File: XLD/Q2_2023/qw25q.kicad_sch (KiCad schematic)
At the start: 521 parts

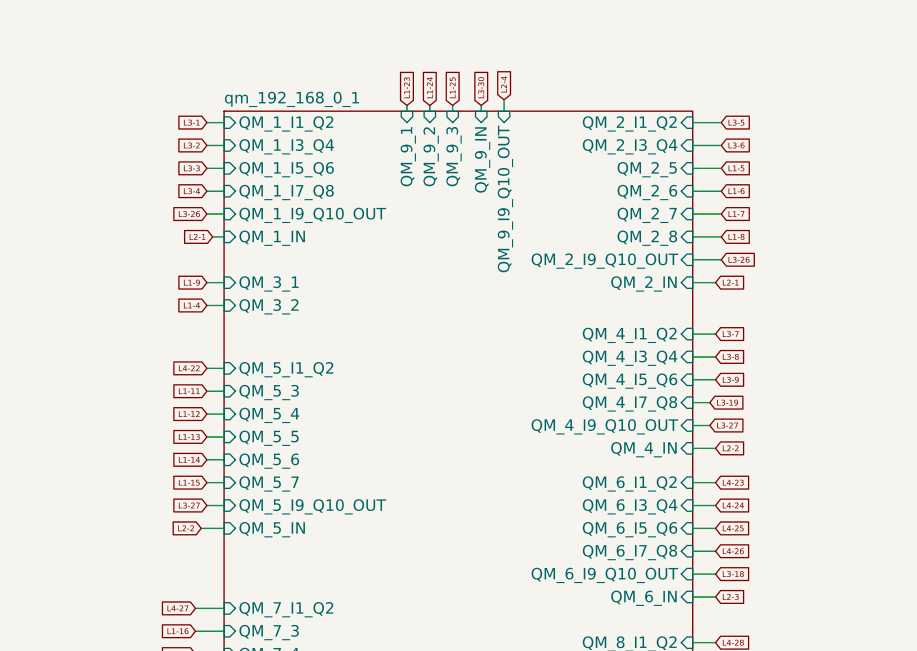
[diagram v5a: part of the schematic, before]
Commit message: connections for qw25q 2 qubit characterization
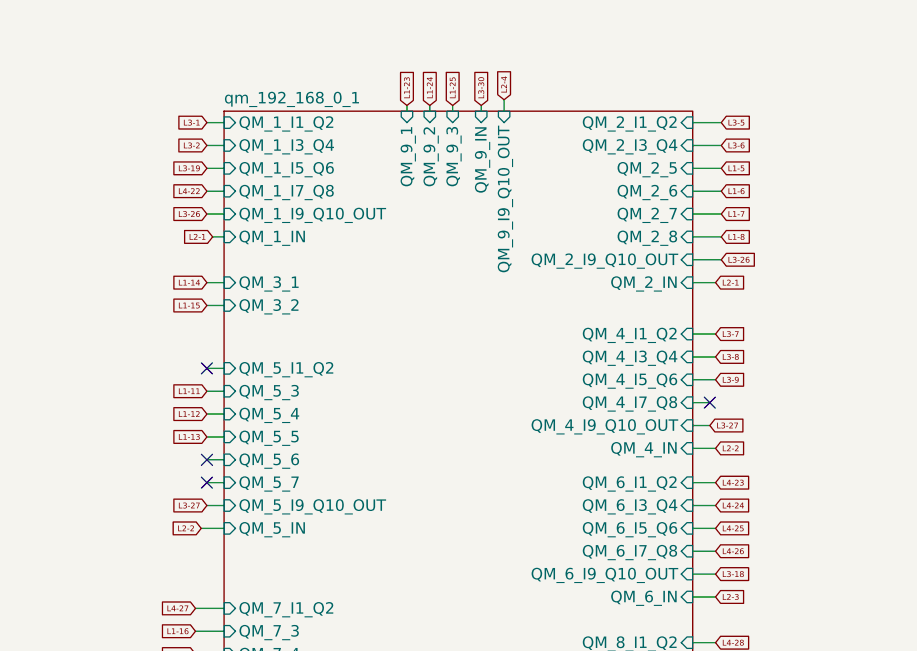
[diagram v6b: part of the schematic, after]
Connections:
- net at EF43.: now also LPF34.; no longer L:96.
- net at EF52.: now also LPF43.; no longer L:104.
- net at EF29.: now also L:5.; no longer LPF20.
- net at EF69.: now also L:153.; no longer LPF60.
- net at Coupler1.: now also L:3.; no longer L:4. (x2)
- net at L:3.: now also TWPA1.; no longer Coupler1.
- net at EF39.: now also LPF30.; no longer L:92.
- net at L:4.: now also Coupler1.; no longer TJI2. (x2)
- net at EF71.: now also LPF62.; no longer L:170.
- net at EF50.: now also L:102.; no longer LPF41.
- net at EF46.: now also L:98.; no longer LPF37.
- net at EF54.: now also L:106.; no longer LPF45.
- net at TJI2.: now also L:4.; no longer L:5.
- net at TWPA1.: now also L:3.; no longer L:2. (x2)
- net at L:3.: now also Coupler1.; no longer TWPA1. (x2)
- net at EF37.: now also L:27.; no longer LPF28.
- net at L:1.: now also TJI1.
- net at TJI1.: now also L:2.; no longer L:1.
- net at L:2.: now also TJI1.; no longer TWPA1. (x2)
- net at TJI1.: now also L:1.; no longer L:2. (x2)
- net at EF70.: now also L:168.; no longer LPF61.
- net at EF33.: now also LPF24.; no longer L:9.
- net at EF31.: now also LPF22.; no longer L:7.
- net at EF64.: now also LPF55.; no longer L:116.
- net at EF27.: now also L:3.; no longer LPF18.
- net at EF62.: now also L:114.; no longer LPF53.
- net at EF68.: now also L:120.; no longer LPF59.
- net at EF66.: now also LPF57.; no longer L:118.
- net at EF41.: now also LPF32.; no longer L:94.
- net at L:4.: now also TJI2.; no longer Coupler1.
- net at EF72.: now also L:174.; no longer LPF63.
- net at L:2.: now also TWPA1.; no longer TJI1.
- net at EF56.: now also L:108.; no longer LPF47.
- net at TJI2.: now also L:5.; no longer L:4.
- net at EF35.: now also L:25.; no longer LPF26.
- net at EF48.: now also L:100.; no longer LPF39.
- net at EF60.: now also LPF51.; no longer L:112.
- net at EF58.: now also LPF49.; no longer L:110.
- new net: EF43., L:96.
- new net: EF52., L:104.
- new net: EF29., LPF20.
- new net: ATT347., ATT348.
- new net: EF69., LPF60.
- new net: Coupler1., L:4. (x2)
- new net: EF39., L:92.
- new net: EF44., LPF35.
- new net: L:4., TJI2.
- new net: EF55., LPF46.
- new net: EF71., L:170.
- new net: EF38., LPF29.
- new net: EF50., LPF41.
- new net: EF46., LPF37.
- new net: EF47., LPF38.
- new net: ATT351., ATT352.
- new net: EF54., LPF45.
- new net: L:5., TJI2.
- new net: L:2., TWPA1. (x3)
- new net: EF37., LPF28.
- new net: EF51., LPF42.
- new net: EF70., LPF61.
- new net: ATT349., ATT350.
- new net: ATT345., ATT346.
- new net: EF65., LPF56.
- new net: EF33., L:9.
- new net: L:6., LX-X2. (x3)
- new net: EF31., L:7.
- new net: EF30., LPF21.
- new net: EF64., L:116.
- new net: EF57., LPF48.
- new net: EF27., LPF18.
- new net: EF49., LPF40.
- new net: EF61., LPF52.
- new net: EF62., LPF53.
- new net: EF68., LPF59.
- new net: EF66., L:118.
- new net: EF41., L:94.
- new net: EF72., LPF63.
- new net: L:2., TJI1.
- new net: EF40., LPF31.
- new net: EF28., LPF19.
- new net: EF56., LPF47.
- new net: EF67., LPF58.
- new net: EF35., LPF26.
- new net: EF63., LPF54.
- new net: EF36., LPF27.
- new net: EF45., LPF36.
- new net: EF53., LPF44.
- new net: EF48., LPF39.
- new net: EF60., L:112.
- new net: EF32., LPF23.
- new net: EF58., L:110.
- new net: EF42., LPF33.
- new net: EF34., LPF25.
- new net: EF59., LPF50.
- no-connect marks 0 -> 4
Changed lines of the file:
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@@
   (junction (at 401.955 142.875) (diameter 0) (color 0 0 0 0)
   )
+  (no_connect (at 730.885 431.8))
+  (no_connect (at 730.885 444.5))
+  (no_connect (at 730.885 441.96))
+  (no_connect (at 786.765 435.61))
   (bus_entry (at 666.75 440.055) (size 2.54 2.54)
     (stroke (width 0) (type default))
@@
     )
   )
-  (global_label "L3-3" (shape input) (at 730.885 409.575 180) (fields_autoplaced)
-    (effects (font (size 0.64 0.64)) (justify right))
-    (property "Intersheetrefs" "${INTERSHEET_REFS}" (at 726.8912 409.575 0)
-      (effects (font (size 1.27 1.27)) (justify right) hide)
-    )
-  )
   (global_label "L2-4" (shape input) (at 763.905 401.955 90) (fields_autoplaced)
     (effects (font (size 0.64 0.64)) (justify left))
@@
     )
   )
-  (global_label "L4-22" (shape input) (at 730.885 431.8 180) (fields_autoplaced)
-    (effects (font (size 0.64 0.64)) (justify right))
-    (property "Intersheetrefs" "${INTERSHEET_REFS}" (at 726.2817 431.8 0)
-      (effects (font (size 1.27 1.27)) (justify right) hide)
-    )
-  )
   (global_label "L2-2_gnd" (shape input) (at 772.795 100.965 180) (fields_autoplaced)
     (effects (font (size 0.64 0.64)) (justify right))
@@
     )
   )
-  (global_label "L1-14" (shape input) (at 730.885 441.96 180) (fields_autoplaced)
-    (effects (font (size 0.64 0.64)) (justify right))
-    (property "Intersheetrefs" "${INTERSHEET_REFS}" (at 726.2817 441.96 0)
-      (effects (font (size 1.27 1.27)) (justify right) hide)
-    )
-  )
   (global_label "L3-24" (shape input) (at 610.235 374.65 90) (fields_autoplaced)
     (effects (font (size 1.27 1.27)) (justify left))
@@
     )
   )
-  (global_label "L3-19" (shape input) (at 786.765 435.61 0) (fields_autoplaced)
-    (effects (font (size 0.64 0.64)) (justify left))
-    (property "Intersheetrefs" "${INTERSHEET_REFS}" (at 791.3683 435.61 0)
-      (effects (font (size 1.27 1.27)) (justify left) hide)
+  (global_label "L3-19" (shape input) (at 730.885 409.575 180) (fields_autoplaced)
+    (effects (font (size 0.64 0.64)) (justify right))
+    (property "Intersheetrefs" "${INTERSHEET_REFS}" (at 726.2817 409.575 0)
+      (effects (font (size 1.27 1.27)) (justify right) hide)
     )
   )
@@
     )
   )
-  (global_label "L1-15" (shape input) (at 730.885 444.5 180) (fields_autoplaced)
+  (global_label "L1-15" (shape input) (at 730.885 424.815 180) (fields_autoplaced)
     (effects (font (size 0.64 0.64)) (justify right))
-    (property "Intersheetrefs" "${INTERSHEET_REFS}" (at 726.2817 444.5 0)
+    (property "Intersheetrefs" "${INTERSHEET_REFS}" (at 726.2817 424.815 0)
       (effects (font (size 1.27 1.27)) (justify right) hide)
     )
@@
     )
   )
+  (global_label "L4-22" (shape input) (at 730.885 412.115 180) (fields_autoplaced)
+    (effects (font (size 0.64 0.64)) (justify right))
+    (property "Intersheetrefs" "${INTERSHEET_REFS}" (at 726.2817 412.115 0)
+      (effects (font (size 1.27 1.27)) (justify right) hide)
+    )
+  )
   (global_label "L1-12" (shape input) (at 730.885 436.88 180) (fields_autoplaced)
     (effects (font (size 0.64 0.64)) (justify right))
@@
     )
   )
+  (global_label "L1-14" (shape input) (at 730.885 422.275 180) (fields_autoplaced)
+    (effects (font (size 0.64 0.64)) (justify right))
+    (property "Intersheetrefs" "${INTERSHEET_REFS}" (at 726.2817 422.275 0)
+      (effects (font (size 1.27 1.27)) (justify right) hide)
+    )
+  )
   (global_label "L3-24" (shape input) (at 646.43 23.495 180) (fields_autoplaced)
     (effects (font (size 1.27 1.27)) (justify right))
@@
     )
   )
-  (global_label "L1-9" (shape input) (at 730.885 422.275 180) (fields_autoplaced)
-    (effects (font (size 0.64 0.64)) (justify right))
-    (property "Intersheetrefs" "${INTERSHEET_REFS}" (at 726.8912 422.275 0)
-      (effects (font (size 1.27 1.27)) (justify right) hide)
-    )
-  )
   (global_label "L1-6" (shape input) (at 788.035 412.115 0) (fields_autoplaced)
     (effects (font (size 0.64 0.64)) (justify left))
@@
     )
   )
-  (global_label "L3-4" (shape input) (at 730.885 412.115 180) (fields_autoplaced)
-    (effects (font (size 0.64 0.64)) (justify right))
-    (property "Intersheetrefs" "${INTERSHEET_REFS}" (at 726.8912 412.115 0)
-      (effects (font (size 1.27 1.27)) (justify right) hide)
-    )
-  )
   (global_label "L2-1" (shape input) (at 731.52 417.195 180) (fields_autoplaced)
     (effects (font (size 0.64 0.64)) (justify right))
@@
     )
   )
-  (global_label "L1-4" (shape input) (at 730.885 424.815 180) (fields_autoplaced)
-    (effects (font (size 0.64 0.64)) (justify right))
-    (property "Intersheetrefs" "${INTERSHEET_REFS}" (at 726.8912 424.815 0)
-      (effects (font (size 1.27 1.27)) (justify right) hide)
-    )
-  )
